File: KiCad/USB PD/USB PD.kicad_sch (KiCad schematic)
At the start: 34 parts, among them J10 CFG, J11 SEL, J12 Conn_01x03_Pin, J12 GND, J18 Conn_01x02_Pin, J7 VCC, J8 ESP32 Jumpers, J8 TX, J9 RX, U1 AO3400A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

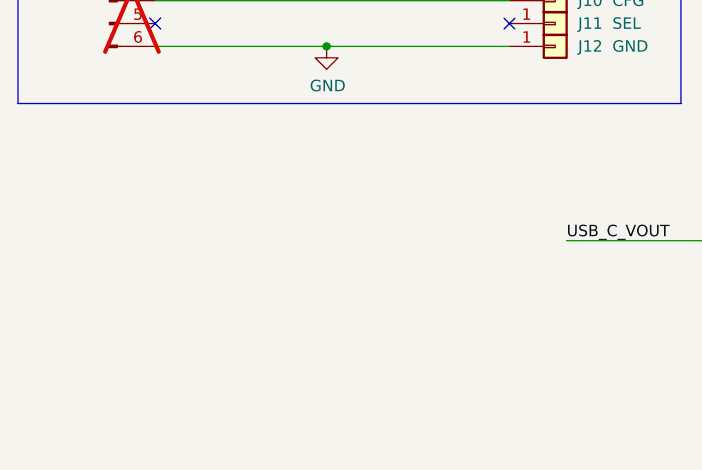
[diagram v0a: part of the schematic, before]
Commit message: Updated USB PD and Driver LED circuit
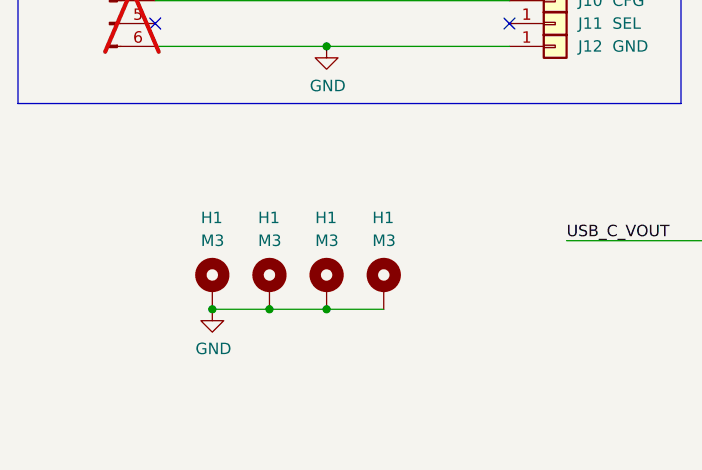
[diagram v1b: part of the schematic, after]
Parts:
- added H1 (x4): M3, Library:MountingHole_3.2mm_M3_Pad_TopBottom, symbol Mechanical:MountingHole_Pad
- TP1, TP3, TP5, TP6: footprint TestPoint:TestPoint_Pad_2.0x2.0mm -> Library:TestPoint_THTPad_2.0x2.0mm_Drill1.0mm
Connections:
- net GND: now also H1.1, H1.1, H1.1, H1.1
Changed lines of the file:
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@@
 (kicad_sch (version 20230121) (generator eeschema)
   (paper "A4")
+  (junction (at 76.2 104.14) (diameter 0) (color 0 0 0 0)
+  )
   (junction (at 135.89 39.37) (diameter 0) (color 0 0 0 0)
   )
@@
   (junction (at 135.89 43.18) (diameter 0) (color 0 0 0 0)
   )
+  (junction (at 63.5 104.14) (diameter 0) (color 0 0 0 0)
+  )
   (junction (at 189.23 17.78) (diameter 0) (color 0 0 0 0)
   )
@@
   )
   (junction (at 137.16 96.52) (diameter 0) (color 0 0 0 0)
+  )
+  (junction (at 69.85 104.14) (diameter 0) (color 0 0 0 0)
   )
   (junction (at 210.82 91.44) (diameter 0) (color 0 0 0 0)
@@
     (stroke (width 0) (type default))
   )
+  (wire (pts (xy 69.85 104.14) (xy 76.2 104.14))
+    (stroke (width 0) (type default))
+  )
   (wire (pts (xy 190.5 99.06) (xy 187.96 99.06))
     (stroke (width 0) (type default))
@@
     (stroke (width 0) (type default))
   )
+  (wire (pts (xy 63.5 104.14) (xy 69.85 104.14))
+    (stroke (width 0) (type default))
+  )
   (wire (pts (xy 245.11 26.67) (xy 245.11 39.37))
     (stroke (width 0) (type default))
@@
   )
   (wire (pts (xy 137.16 96.52) (xy 127 96.52))
+    (stroke (width 0) (type default))
+  )
+  (wire (pts (xy 76.2 104.14) (xy 82.55 104.14))
     (stroke (width 0) (type default))
   )
@@
   (label "USB_C_VIN" (at 160.02 60.96 0) (fields_autoplaced)
     (effects (font (size 1.27 1.27)) (justify left bottom))
+  )
+  (symbol (lib_id "Mechanical:MountingHole_Pad") (at 63.5 101.6 0) (unit 1)
+    (in_bom yes) (on_board yes) (dnp no)
+    (property "Reference" "H1" (at 62.23 93.98 0)
+      (effects (font (size 1.27 1.27)) (justify left))
+    )
+    (property "Value" "M3" (at 62.23 96.52 0)
+      (effects (font (size 1.27 1.27)) (justify left))
+    )
+    (property "Footprint" "Library:MountingHole_3.2mm_M3_Pad_TopBottom" (at 63.5 101.6 0)
+      (effects (font (size 1.27 1.27)) hide)
+    )
+    (property "Datasheet" "~" (at 63.5 101.6 0)
+      (effects (font (size 1.27 1.27)) hide)
+    )
+    (pin "1")
+    (instances
+      (project "Retro Display Module"
+        (path "/046eef48-6d3f-4288-a12a-fc20b7e12e30"
+          (reference "H1") (unit 1)
+        )
+      )
+      (project "USB PD"
+        (path "/339a92df-fdbb-48aa-b235-136f297cfd8f"
+          (reference "H1") (unit 1)
+        )
+      )
+    )
   )
   (symbol (lib_id "Device:C_Small") (at 189.23 21.59 0) (unit 1)
@@
       (effects (font (size 1.27 1.27)) (justify left))
     )
-    (property "Footprint" "TestPoint:TestPoint_Pad_2.0x2.0mm" (at 191.77 17.78 0)
+    (property "Footprint" "Library:TestPoint_THTPad_2.0x2.0mm_Drill1.0mm" (at 191.77 17.78 0)
       (effects (font (size 1.27 1.27)) hide)
     )
@@
     )
   )
+  (symbol (lib_id "Mechanical:MountingHole_Pad") (at 82.55 101.6 0) (unit 1)
+    (in_bom yes) (on_board yes) (dnp no)
+    (property "Reference" "H1" (at 81.28 93.98 0)
+      (effects (font (size 1.27 1.27)) (justify left))
+    )
+    (property "Value" "M3" (at 81.28 96.52 0)
+      (effects (font (size 1.27 1.27)) (justify left))
+    )
+    (property "Footprint" "Library:MountingHole_3.2mm_M3_Pad_TopBottom" (at 82.55 101.6 0)
+      (effects (font (size 1.27 1.27)) hide)
+    )
+    (property "Datasheet" "~" (at 82.55 101.6 0)
+      (effects (font (size 1.27 1.27)) hide)
+    )
+    (pin "1")
+    (instances
+      (project "Retro Display Module"
+        (path "/046eef48-6d3f-4288-a12a-fc20b7e12e30"
+          (reference "H1") (unit 1)
+        )
+      )
+      (project "USB PD"
+        (path "/339a92df-fdbb-48aa-b235-136f297cfd8f"
+          (reference "H4") (unit 1)
+        )
+      )
+    )
+  )
   (symbol (lib_id "power:GND") (at 189.23 24.13 0) (unit 1)
     (in_bom yes) (on_board yes) (dnp no)
@@
       (effects (font (size 1.27 1.27)) (justify left))
     )
-    (property "Footprint" "TestPoint:TestPoint_Pad_2.0x2.0mm" (at 142.24 96.52 0)
+    (property "Footprint" "Library:TestPoint_THTPad_2.0x2.0mm_Drill1.0mm" (at 142.24 96.52 0)
       (effects (font (size 1.27 1.27)) hide)
     )
@@
       (effects (font (size 1.27 1.27)) (justify left))
     )
-    (property "Footprint" "TestPoint:TestPoint_Pad_2.0x2.0mm" (at 127 43.18 0)
+    (property "Footprint" "Library:TestPoint_THTPad_2.0x2.0mm_Drill1.0mm" (at 127 43.18 0)
       (effects (font (size 1.27 1.27)) hide)
     )
@@
     )
   )
+  (symbol (lib_id "Mechanical:MountingHole_Pad") (at 76.2 101.6 0) (unit 1)
+    (in_bom yes) (on_board yes) (dnp no)
+    (property "Reference" "H1" (at 74.93 93.98 0)
+      (effects (font (size 1.27 1.27)) (justify left))
+    )
+    (property "Value" "M3" (at 74.93 96.52 0)
+      (effects (font (size 1.27 1.27)) (justify left))
+    )
+    (property "Footprint" "Library:MountingHole_3.2mm_M3_Pad_TopBottom" (at 76.2 101.6 0)
+      (effects (font (size 1.27 1.27)) hide)
+    )
+    (property "Datasheet" "~" (at 76.2 101.6 0)
+      (effects (font (size 1.27 1.27)) hide)
+    )
+    (pin "1")
+    (instances
+      (project "Retro Display Module"
+        (path "/046eef48-6d3f-4288-a12a-fc20b7e12e30"
+          (reference "H1") (unit 1)
+        )
+      )
+      (project "USB PD"
+        (path "/339a92df-fdbb-48aa-b235-136f297cfd8f"
+          (reference "H3") (unit 1)
+        )
+      )
+    )
+  )
   (symbol (lib_id "Connector_Generic:Conn_01x01") (at 101.6 69.85 0) (unit 1)
     (in_bom yes) (on_board yes) (dnp no)
@@
     )
   )
+  (symbol (lib_id "Mechanical:MountingHole_Pad") (at 69.85 101.6 0) (unit 1)
+    (in_bom yes) (on_board yes) (dnp no)
+    (property "Reference" "H1" (at 68.58 93.98 0)
+      (effects (font (size 1.27 1.27)) (justify left))
+    )
+    (property "Value" "M3" (at 68.58 96.52 0)
+      (effects (font (size 1.27 1.27)) (justify left))
+    )
+    (property "Footprint" "Library:MountingHole_3.2mm_M3_Pad_TopBottom" (at 69.85 101.6 0)
+      (effects (font (size 1.27 1.27)) hide)
+    )
+    (property "Datasheet" "~" (at 69.85 101.6 0)
+      (effects (font (size 1.27 1.27)) hide)
+    )
+    (pin "1")
+    (instances
+      (project "Retro Display Module"
+        (path "/046eef48-6d3f-4288-a12a-fc20b7e12e30"
+          (reference "H1") (unit 1)
+        )
+      )
+      (project "USB PD"
+        (path "/339a92df-fdbb-48aa-b235-136f297cfd8f"
+          (reference "H2") (unit 1)
+        )
+      )
+    )
+  )
   (symbol (lib_id "Connector:Conn_01x02_Pin") (at 114.3 38.1 90) (mirror x) (unit 1)
     (in_bom yes) (on_board yes) (dnp yes)
@@
     )
   )
+  (symbol (lib_id "power:GND") (at 63.5 104.14 0) (unit 1)
+    (in_bom yes) (on_board yes) (dnp no)
+    (property "Reference" "#PWR01" (at 63.5 110.49 0)
+      (effects (font (size 1.27 1.27)) hide)
+    )
+    (property "Value" "GND" (at 63.627 108.5342 0)
+      (effects (font (size 1.27 1.27)))
+    )
+    (property "Footprint" "" (at 63.5 104.14 0)
+      (effects (font (size 1.27 1.27)) hide)
+    )
+    (property "Datasheet" "" (at 63.5 104.14 0)
+      (effects (font (size 1.27 1.27)) hide)
+    )
+    (pin "1")
+    (instances
+      (project "Retro Display Module"
+        (path "/046eef48-6d3f-4288-a12a-fc20b7e12e30/ac319926-f718-40b4-a3fe-2bfb67ca9f6d"
+          (reference "#PWR01") (unit 1)
+        )
+        (path "/046eef48-6d3f-4288-a12a-fc20b7e12e30"
+          (reference "#PWR021") (unit 1)
+        )
+      )
+      (project "USB PD"
+        (path "/339a92df-fdbb-48aa-b235-136f297cfd8f"
+          (reference "#PWR015") (unit 1)
+        )
+      )
+      (project "IP2721-USB-C-breakout"
+        (path "/5bfe13c5-4fd6-45ac-8bff-6f389cf1f1b4/00000000-0000-0000-0000-00006147c43f"
+          (reference "#PWR0107") (unit 1)
+        )
+      )
+    )
+  )
   (symbol (lib_id "Connector:TestPoint") (at 201.93 106.68 0) (mirror x) (unit 1)
     (in_bom yes) (on_board yes) (dnp no)
@@
       (effects (font (size 1.27 1.27)) (justify left))
     )
-    (property "Footprint" "TestPoint:TestPoint_Pad_2.0x2.0mm" (at 207.01 106.68 0)
-      (effects (font (size 1.27 1.27)) hide)
-    )
+    (property "Footprint" "Library:TestPoint_THTPad_2.0x2.0mm_Drill1.0mm" (at 207.01 106.68 0)
+      (effects (font (size 1.27 1.27)) hide)
+    )

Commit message: Begin STM32 Programming
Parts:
- H1: now not fitted; now left out of the parts list
- J12, J18, J8, TP1, TP3, TP5, TP6: now left out of the parts list
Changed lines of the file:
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@@
   )
   (symbol (lib_id "Mechanical:MountingHole_Pad") (at 63.5 101.6 0) (unit 1)
-    (in_bom yes) (on_board yes) (dnp no)
+    (in_bom no) (on_board yes) (dnp yes)
     (property "Reference" "H1" (at 62.23 93.98 0)
       (effects (font (size 1.27 1.27)) (justify left))
@@
   )
   (symbol (lib_id "Connector:Conn_01x02_Pin") (at 162.56 105.41 0) (mirror y) (unit 1)
-    (in_bom yes) (on_board yes) (dnp yes)
+    (in_bom no) (on_board yes) (dnp yes)
     (property "Reference" "J18" (at 166.37 107.95 0)
       (effects (font (size 1.27 1.27)))
@@
   )
   (symbol (lib_id "Connector:TestPoint") (at 196.85 17.78 0) (mirror y) (unit 1)
-    (in_bom yes) (on_board yes) (dnp no) (fields_autoplaced)
+    (in_bom no) (on_board yes) (dnp no) (fields_autoplaced)
     (property "Reference" "TP3" (at 195.453 13.8343 0)
       (effects (font (size 1.27 1.27)) (justify left))
@@
   )
   (symbol (lib_id "Connector:Conn_01x02_Pin") (at 88.9 57.15 90) (mirror x) (unit 1)
-    (in_bom yes) (on_board yes) (dnp yes)
+    (in_bom no) (on_board yes) (dnp yes)
     (property "Reference" "J18" (at 91.44 53.34 90)
       (effects (font (size 1.27 1.27)))
@@
   )
   (symbol (lib_id "Connector:Conn_01x03_Pin") (at 181.61 69.85 90) (unit 1)
-    (in_bom yes) (on_board yes) (dnp yes) (fields_autoplaced)
+    (in_bom no) (on_board yes) (dnp yes) (fields_autoplaced)
     (property "Reference" "J12" (at 181.61 71.5217 90)
       (effects (font (size 1.27 1.27)))
@@
   )
   (symbol (lib_id "Mechanical:MountingHole_Pad") (at 82.55 101.6 0) (unit 1)
-    (in_bom yes) (on_board yes) (dnp no)
+    (in_bom no) (on_board yes) (dnp yes)
     (property "Reference" "H1" (at 81.28 93.98 0)
       (effects (font (size 1.27 1.27)) (justify left))
@@
   )
   (symbol (lib_id "Connector:TestPoint") (at 137.16 96.52 0) (unit 1)
-    (in_bom yes) (on_board yes) (dnp no)
+    (in_bom no) (on_board yes) (dnp no)
     (property "Reference" "TP6" (at 138.557 92.5743 0)
       (effects (font (size 1.27 1.27)) (justify left))
@@
   )
   (symbol (lib_id "Connector:TestPoint") (at 132.08 43.18 0) (mirror y) (unit 1)
-    (in_bom yes) (on_board yes) (dnp no) (fields_autoplaced)
+    (in_bom no) (on_board yes) (dnp no) (fields_autoplaced)
     (property "Reference" "TP1" (at 130.683 39.2343 0)
       (effects (font (size 1.27 1.27)) (justify left))
@@
   )
   (symbol (lib_id "Connector:Conn_01x02_Pin") (at 224.79 86.36 90) (mirror x) (unit 1)
-    (in_bom yes) (on_board yes) (dnp yes)
+    (in_bom no) (on_board yes) (dnp yes)
     (property "Reference" "J18" (at 227.33 82.55 0)
       (effects (font (size 1.27 1.27)))
@@
   )
   (symbol (lib_id "Connector:Conn_01x06_Pin") (at 52.07 67.31 0) (unit 1)
-    (in_bom yes) (on_board yes) (dnp yes)
+    (in_bom no) (on_board yes) (dnp yes)
     (property "Reference" "J8" (at 52.07 57.15 0)
       (effects (font (size 1.27 1.27)))
@@
   )
   (symbol (lib_id "Mechanical:MountingHole_Pad") (at 76.2 101.6 0) (unit 1)
-    (in_bom yes) (on_board yes) (dnp no)
+    (in_bom no) (on_board yes) (dnp yes)
     (property "Reference" "H1" (at 74.93 93.98 0)
       (effects (font (size 1.27 1.27)) (justify left))
@@
   )
   (symbol (lib_id "Mechanical:MountingHole_Pad") (at 69.85 101.6 0) (unit 1)
-    (in_bom yes) (on_board yes) (dnp no)
+    (in_bom no) (on_board yes) (dnp yes)
     (property "Reference" "H1" (at 68.58 93.98 0)
       (effects (font (size 1.27 1.27)) (justify left))
@@
   )
   (symbol (lib_id "Connector:Conn_01x02_Pin") (at 114.3 38.1 90) (mirror x) (unit 1)
-    (in_bom yes) (on_board yes) (dnp yes)
+    (in_bom no) (on_board yes) (dnp yes)
     (property "Reference" "J18" (at 116.84 34.29 0)
       (effects (font (size 1.27 1.27)))
@@
   )
   (symbol (lib_id "Connector:Conn_01x02_Pin") (at 124.46 91.44 90) (mirror x) (unit 1)
-    (in_bom yes) (on_board yes) (dnp yes)
+    (in_bom no) (on_board yes) (dnp yes)
     (property "Reference" "J18" (at 127 87.63 0)
       (effects (font (size 1.27 1.27)))
@@
   )
   (symbol (lib_id "Connector:TestPoint") (at 201.93 106.68 0) (mirror x) (unit 1)
-    (in_bom yes) (on_board yes) (dnp no)
+    (in_bom no) (on_board yes) (dnp no)
     (property "Reference" "TP5" (at 203.327 110.6257 0)
       (effects (font (size 1.27 1.27)) (justify left))

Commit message: Final Commit for 4022S
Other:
- moved on the sheet: C1, C2, C4, C5, D23, H1, J10, J11, J12, J18, J7, J8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

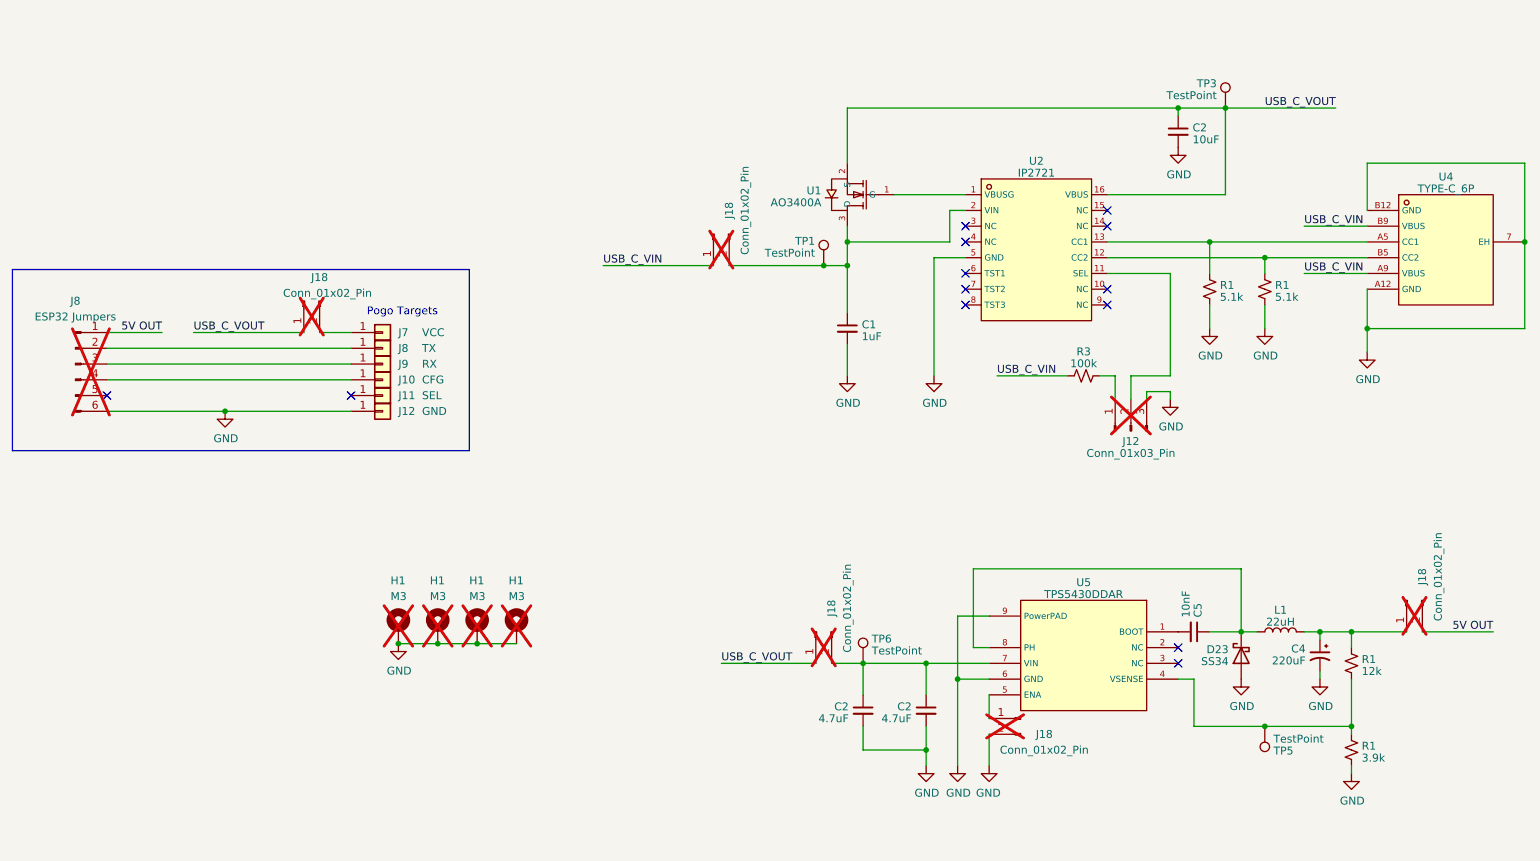
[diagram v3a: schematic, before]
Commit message: Updated Schematics and Added Reverse polarity protection
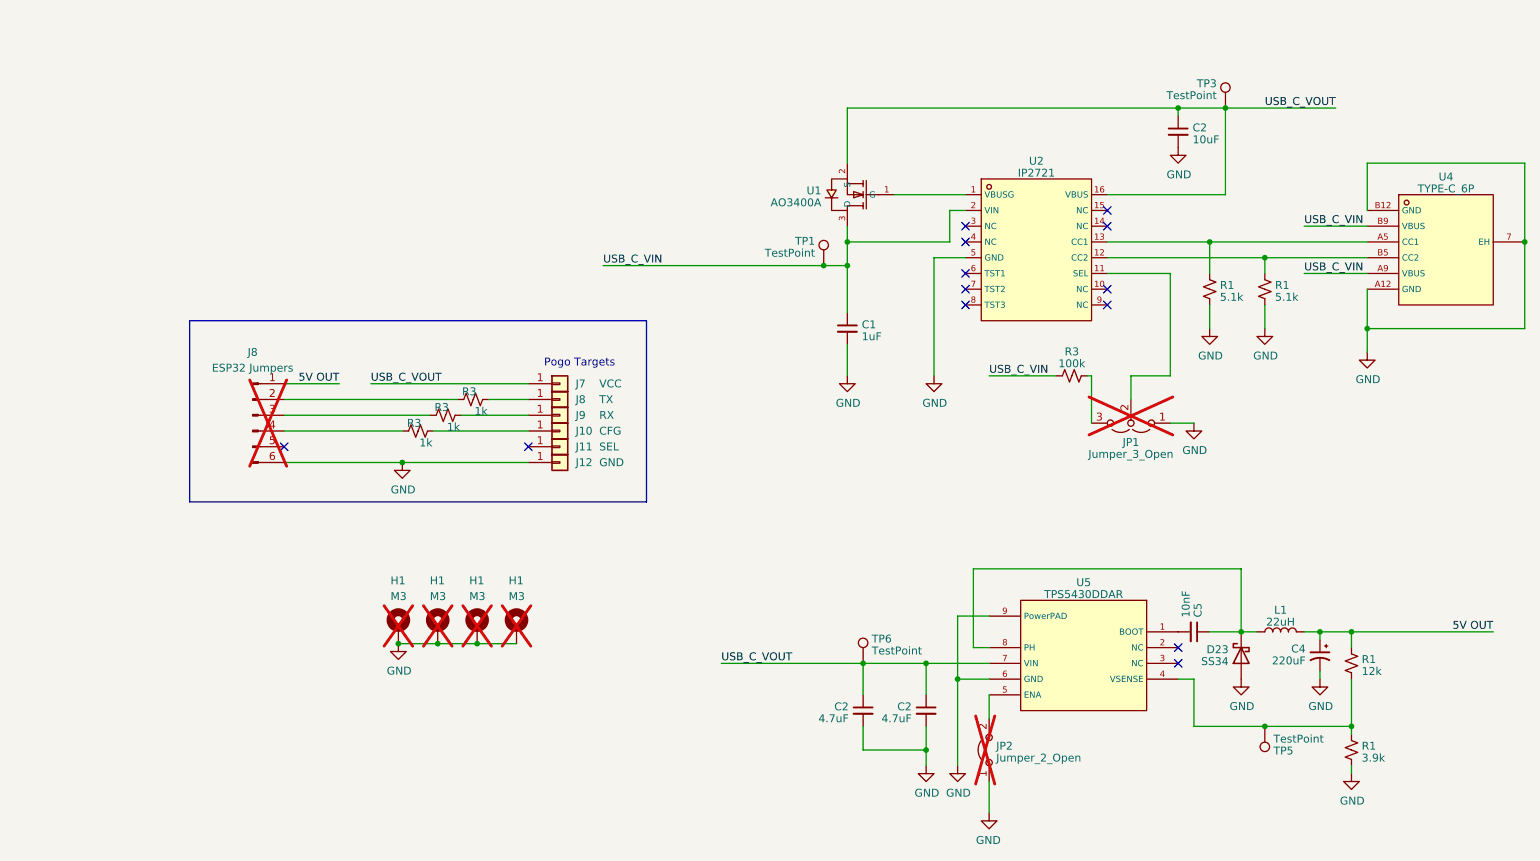
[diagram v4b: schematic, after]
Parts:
- removed J12: Conn_01x03_Pin, Connector_PinHeader_2.54mm:PinHeader_1x03_P2.54mm_Vertical, symbol Connector:Conn_01x03_Pin
- removed J18 (x5): Conn_01x02_Pin, Connector_PinHeader_2.54mm:PinHeader_1x02_P2.54mm_Vertical, symbol Connector:Conn_01x02_Pin
- added JP1: Jumper_3_Open, Jumper:SolderJumper-3_P1.3mm_Open_RoundedPad1.0x1.5mm_NumberLabels, symbol Jumper:Jumper_3_Open
- added JP2: Jumper_2_Open, Jumper:SolderJumper-2_P1.3mm_Open_RoundedPad1.0x1.5mm, symbol Jumper:Jumper_2_Open
- added R3 (x3): 1k, Library:R_0402_1005Metric_Pad0.72x0.64mm_HandSolder, symbol Device:R_Small_US
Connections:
- net 5V OUT: now also C4.1, L1.2, R1.1
- net GND: now also JP1.1 (A), JP2.1 (A)
- net USB_C_VIN: now also C1.1, TP1.1, U1.3 (D), U2.2 (VIN)
- net USB_C_VOUT: now also C2.1, C2.1, J7.1 (Pin_1), TP6.1, U5.7 (VIN)
- net at U5.5 (ENA): now also JP2.2 (B)
- net at R3.2: now also JP1.3 (B)
- net at U2.11 (SEL): now also JP1.2 (C)
- net at J8.2 (Pin_2): now also R3.2; no longer J8.1 (Pin_1)
- net at J9.1 (Pin_1): now also R3.1; no longer J8.3 (Pin_3)
- net at J10.1 (Pin_1): now also R3.1; no longer J8.4 (Pin_4)
- new net: J8.4 (Pin_4), R3.2
- new net: J8.3 (Pin_3), R3.2
- new net: J8.1 (Pin_1), R3.1
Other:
- moved on the sheet: J10, J11, J12, J7, J8, J9, R3
